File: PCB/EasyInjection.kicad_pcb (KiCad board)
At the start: 2 copper layers, 61.2 x 37.1 mm, 13 parts, among them J1 Conn_02x05_Top_Bottom

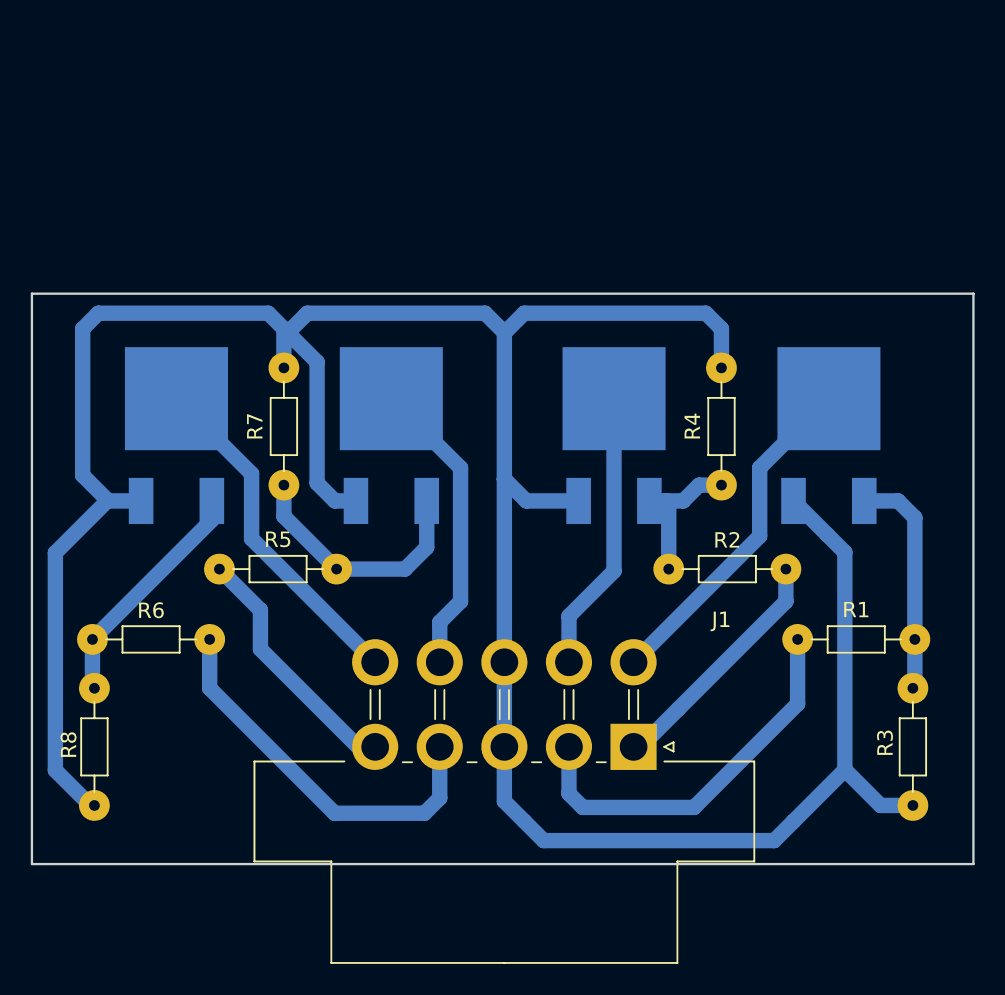
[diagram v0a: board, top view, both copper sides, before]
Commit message: Changed to 5 channels
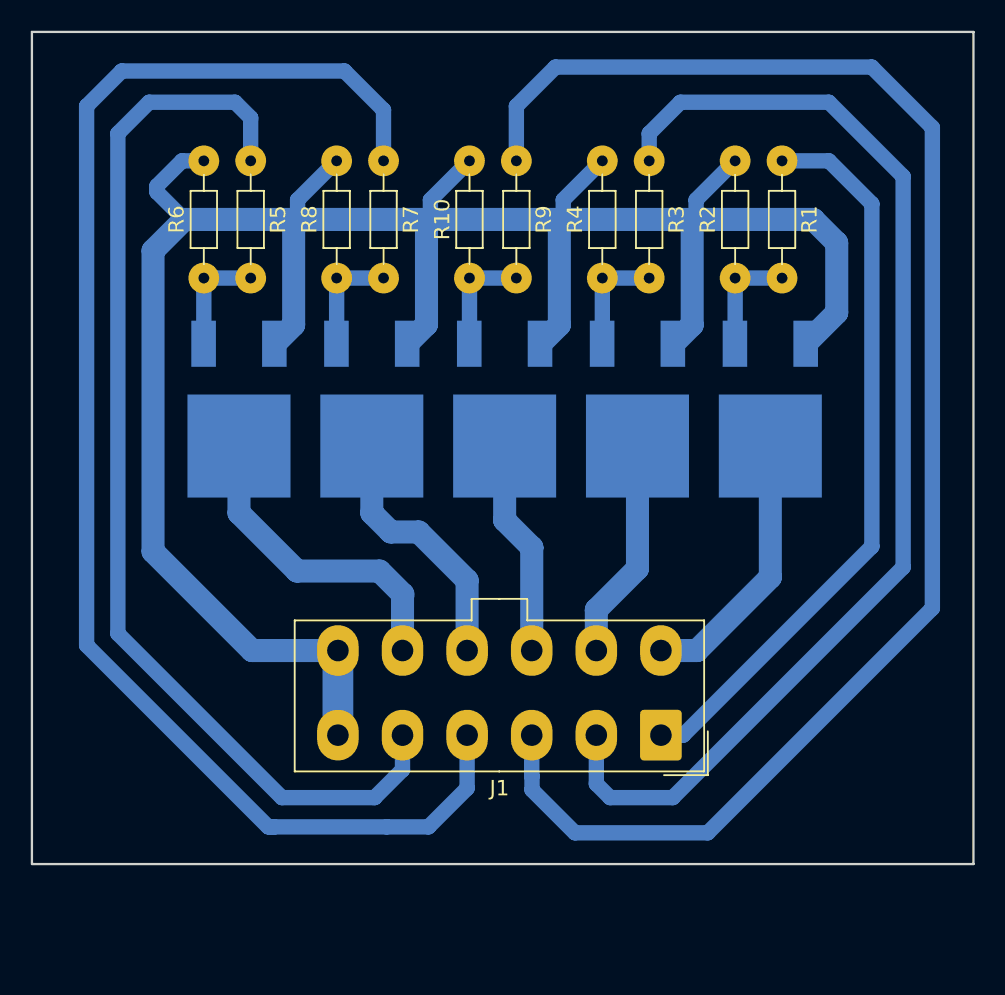
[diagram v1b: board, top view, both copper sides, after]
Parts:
- added R10: 100k, VND5N07:R_Axial_DIN0204_L3.6mm_D1.6mm_P7.62mm_Horizontal, F.Cu at (142.5, 77.0)
- added R9: 1k, VND5N07:R_Axial_DIN0204_L3.6mm_D1.6mm_P7.62mm_Horizontal, F.Cu at (145.5, 77.0)
- added S5: VND5N07, VND5N07:VND5N07_TO-252-(DPAK), B.Cu at (127.5, 89.9)
- J1: value Conn_02x05_Top_Bottom -> Conn_02x06_Top_Bottom; footprint Connectors_Molex:Molex_MiniFit-JR-5569-10A1_2x05x4.20mm_Angled -> Connector_Molex:Molex_Mini-Fit_Jr_5566-12A_2x06_P4.20mm_Vertical
- R2, R6: value 1k -> 100k
- R3, R7: value 100k -> 1k
- moved R3 31.7 mm to (154.2, 77.0), turned to 90 degrees
- moved R8 31.0 mm to (133.9, 77.0), turned to 90 degrees
- moved R1 25.0 mm to (162.8, 77.0), turned to 90 degrees
- moved R6 24.6 mm to (125.2, 77.0), turned to 90 degrees
- moved R5 19.7 mm to (128.3, 77.0), turned to 90 degrees
- moved R2 19.4 mm to (159.8, 77.0), turned to 90 degrees
- moved R4 15.5 mm to (151.1, 77.0)
- moved R7 14.9 mm to (136.9, 77.0)
- moved S4 14.5 mm to (136.1, 89.9), turned to 90 degrees
- moved S3 10.2 mm to (144.8, 89.9), turned to 90 degrees
- moved S1 8.04 mm to (162.1, 89.9), turned to 90 degrees
- moved S2 7.24 mm to (153.4, 89.9), turned to 90 degrees
- moved J1 1.93 mm to (154.9, 106.7)
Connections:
- J1 pad 1: CTRL_2 -> CTRL_1
- J1 pad 2: CTRL_1 -> CTRL_2
- J1 pad 3: GNDPWR -> CTRL_3
- J1 pad 5: CTRL_3 -> CTRL_5
- J1 pad 6: OUT_1 -> GNDPWR
- J1 pad 7: OUT_2 -> OUT_1
- J1 pad 8: GNDPWR -> OUT_2
- R2 pad 1: Net-(R2-Pad1) -> Net-(R1-Pad1)
- R2 pad 2: CTRL_2 -> GNDPWR
- R3 pad 1: Net-(R1-Pad1) -> Net-(R3-Pad1)
- R3 pad 2: GNDPWR -> CTRL_2
- R4 pad 1: Net-(R2-Pad1) -> Net-(R3-Pad1)
- R5 pad 2: CTRL_3 -> CTRL_5
- R6 pad 1: Net-(R6-Pad1) -> Net-(R5-Pad1)
- R6 pad 2: CTRL_4 -> GNDPWR
- R7 pad 1: Net-(R5-Pad1) -> Net-(R7-Pad1)
- R7 pad 2: GNDPWR -> CTRL_4
- R8 pad 1: Net-(R6-Pad1) -> Net-(R7-Pad1)
- S2 pad 1: Net-(R2-Pad1) -> Net-(R3-Pad1)
- S3 pad 1: Net-(R5-Pad1) -> Net-(R10-Pad1)
- S4 pad 1: Net-(R6-Pad1) -> Net-(R7-Pad1)
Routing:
- net CTRL_3: track 16.4 -> 101.3 mm
- net CTRL_5: track 0.00 -> 71.1 mm
- net CTRL_4: track 25.2 -> 94.1 mm
- net CTRL_2: track 15.9 -> 76.2 mm
- net GNDPWR: track 184.9 -> 154.5 mm
- net OUT_5: track 0.00 -> 23.0 mm
- net CTRL_1: track 26.1 -> 48.1 mm
- net Net-(R6-Pad1): track 15.4 -> 0.00 mm
- net Net-(R2-Pad1): track 9.61 -> 0.00 mm
- net Net-(R5-Pad1): track 16.3 -> 7.33 mm
- net Net-(R1-Pad1): track 14.9 -> 7.33 mm
- net Net-(R7-Pad1): track 0.00 -> 7.33 mm
- net Net-(R10-Pad1): track 0.00 -> 7.33 mm
- net Net-(R3-Pad1): track 0.00 -> 7.33 mm
- net OUT_4: track 22.5 -> 16.9 mm
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- removed copper zone on B.Cu, net GNDPWR
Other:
- board size 61.2 x 37.1 mm -> 61.2 x 54.1 mm
- net class Default: clearance 0.5 -> 0.9
- net class power added: clearance 0.9, trace_width 1.5, via_dia 0.6, via_drill 0.4
- rule trace_clearance: 0.5 -> 0.9
